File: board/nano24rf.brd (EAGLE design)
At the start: 17.8 x 40.3 mm, 18 parts

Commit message: ready for raw jumoper"
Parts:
- removed SJ4: JUMPER-PAD-3-2OF3_NC_BY_TRACE_LARGE, ATTAMI-V0.00:PAD-JUMPER-3-2OF3_NC_BY_TRACE_YES_SILK_LARGE
- added SJ2: (no value), microbuilder:SOLDERJUMPER_REFLOW
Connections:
- removed net N$6: D1.1, D2.1, FET1.1, FET2.1, SJ4.2
- net RAW: now also SJ2.1; no longer SJ4.3
- net VOUT: now also D1.1, D2.1, FET1.1, FET2.1, SJ2.2; no longer SJ4.1
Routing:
- net N$6: track 14.6 -> 0.00 mm
- net RAW: track 37.7 -> 32.9 mm
- net VOUT: track 22.8 -> 24.4 mm
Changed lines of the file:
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@@
 <wire x1="0" y1="40.31" x2="0" y2="0" width="0" layer="20"/>
 <text x="4.445" y="30.48" size="1.27" layer="21" font="vector">SEshenkar</text>
-<text x="5.715" y="37.973" size="1.27" layer="21" font="vector">nano24RF</text>
-<text x="10.795" y="36.703" size="0.8128" layer="21" font="vector">v1</text>
+<text x="4.445" y="37.973" size="1.27" layer="21" font="vector">nano24RF</text>
+<text x="10.16" y="36.703" size="0.8128" layer="21" font="vector">v1</text>
 <wire x1="6.477" y1="0.889" x2="6.985" y2="0.889" width="0.254" layer="21"/>
 <wire x1="7.493" y1="0.889" x2="6.985" y2="0.889" width="0.254" layer="21"/>
@@
 <attribute name="VALUE" x="13.335" y="39.37" size="0.4064" layer="27" ratio="10" rot="R270"/>
 </element>
-<element name="SJ4" library="ATTAMI-V0.00" package="PAD-JUMPER-3-2OF3_NC_BY_TRACE_YES_SILK_LARGE" value="JUMPER-PAD-3-2OF3_NC_BY_TRACE_LARGE" x="8.255" y="10.795" smashed="yes" rot="R180">
-<attribute name="NAME" x="10.922" y="12.065" size="1.016" layer="25" font="vector" ratio="10" rot="R270"/>
-<attribute name="VALUE" x="8.3551" y="10.795" size="0.02" layer="27" rot="R180"/>
-</element>
+<element name="SJ2" library="microbuilder" package="SOLDERJUMPER_REFLOW" value="" x="5.08" y="-1.905"/>
 </elements>
 <signals>
@@
 <contactref element="JP1" pad="15"/>
 <contactref element="SJ1" pad="1"/>
-<contactref element="SJ4" pad="3"/>
 <wire x1="8.255" y1="28.702" x2="8.255" y2="28.31" width="0.4064" layer="1"/>
 <wire x1="8.255" y1="28.31" x2="9.895" y2="26.67" width="0.4064" layer="1"/>
@@
 <wire x1="1.27" y1="2.54" x2="5.715" y2="8.89" width="1.016" layer="16"/>
 <via x="5.715" y="8.89" extent="1-16" drill="0.6" shape="square"/>
-<wire x1="5.715" y1="8.89" x2="6.731" y2="10.795" width="1.016" layer="1" curve="13.839067"/>
-<wire x1="6.731" y1="10.795" x2="8.001" y2="13.081" width="0.6096" layer="1" curve="-15.803299"/>
 <via x="8.001" y="13.081" extent="1-16" drill="0.6" shape="square"/>
 <wire x1="8.001" y1="13.081" x2="8.001" y2="15.113" width="0.6096" layer="16" curve="73.912494"/>
@@
 <wire x1="11.049" y1="28.956" x2="11.049" y2="27.824" width="0.6096" layer="1"/>
 <wire x1="11.049" y1="27.824" x2="9.895" y2="26.67" width="0.6096" layer="1"/>
+<contactref element="SJ2" pad="1"/>
+<wire x1="5.715" y1="8.89" x2="8.001" y2="13.081" width="0" layer="19" extent="1-1"/>
+<wire x1="4.318" y1="-1.905" x2="1.27" y2="2.54" width="0" layer="19" extent="1-1"/>
 </signal>
 <signal name="N$2">
@@
 <contactref element="C2" pad="1"/>
 <contactref element="R4" pad="1"/>
-<contactref element="SJ4" pad="1"/>
 <wire x1="5.3" y1="24.765" x2="8.1" y2="24.765" width="0.4064" layer="1"/>
 <wire x1="8.1" y1="24.765" x2="10.16" y2="25.03" width="0.4064" layer="1"/>
@@
 <wire x1="13.208" y1="22.479" x2="13.208" y2="21.336" width="0.6096" layer="1" curve="13.746918"/>
 <wire x1="8.89" y1="17.78" x2="9.525" y2="13.081" width="0.6096" layer="1"/>
-<wire x1="9.525" y1="13.081" x2="9.779" y2="10.795" width="0.6096" layer="1" curve="-2.71172"/>
+<contactref element="D2" pad="1"/>
+<contactref element="FET2" pad="1"/>
+<wire x1="10.085" y1="6.35" x2="10.795" y2="2.54" width="1.016" layer="1"/>
+<contactref element="FET1" pad="1"/>
+<contactref element="D1" pad="1"/>
+<contactref element="SJ2" pad="2"/>
+<wire x1="10.085" y1="6.35" x2="9.525" y2="13.081" width="0" layer="19" extent="1-1"/>
+<wire x1="7.695" y1="6.35" x2="10.085" y2="6.35" width="0" layer="19" extent="1-1"/>
+<wire x1="6.985" y1="2.54" x2="10.795" y2="2.54" width="0" layer="19" extent="1-1"/>
+<wire x1="5.842" y1="-1.905" x2="6.985" y2="2.54" width="0" layer="19" extent="1-1"/>
 </signal>
 <signal name="N$7">
@@
 <wire x1="15.24" y1="8.509" x2="16.51" y2="7.62" width="0.4064" layer="16" curve="82.225714"/>
 </signal>
-<signal name="N$6">
-<contactref element="FET1" pad="1"/>
-<contactref element="D1" pad="1"/>
-<contactref element="SJ4" pad="2"/>
-<contactref element="D2" pad="1"/>
-<contactref element="FET2" pad="1"/>
-<wire x1="8.255" y1="10.795" x2="7.695" y2="6.35" width="1.016" layer="1"/>
-<wire x1="7.695" y1="6.35" x2="10.085" y2="6.35" width="1.016" layer="1"/>
-<wire x1="10.085" y1="6.35" x2="10.795" y2="2.54" width="1.016" layer="1"/>
-<wire x1="10.795" y1="2.54" x2="6.985" y2="2.54" width="1.016" layer="1"/>
-</signal>
 </signals>

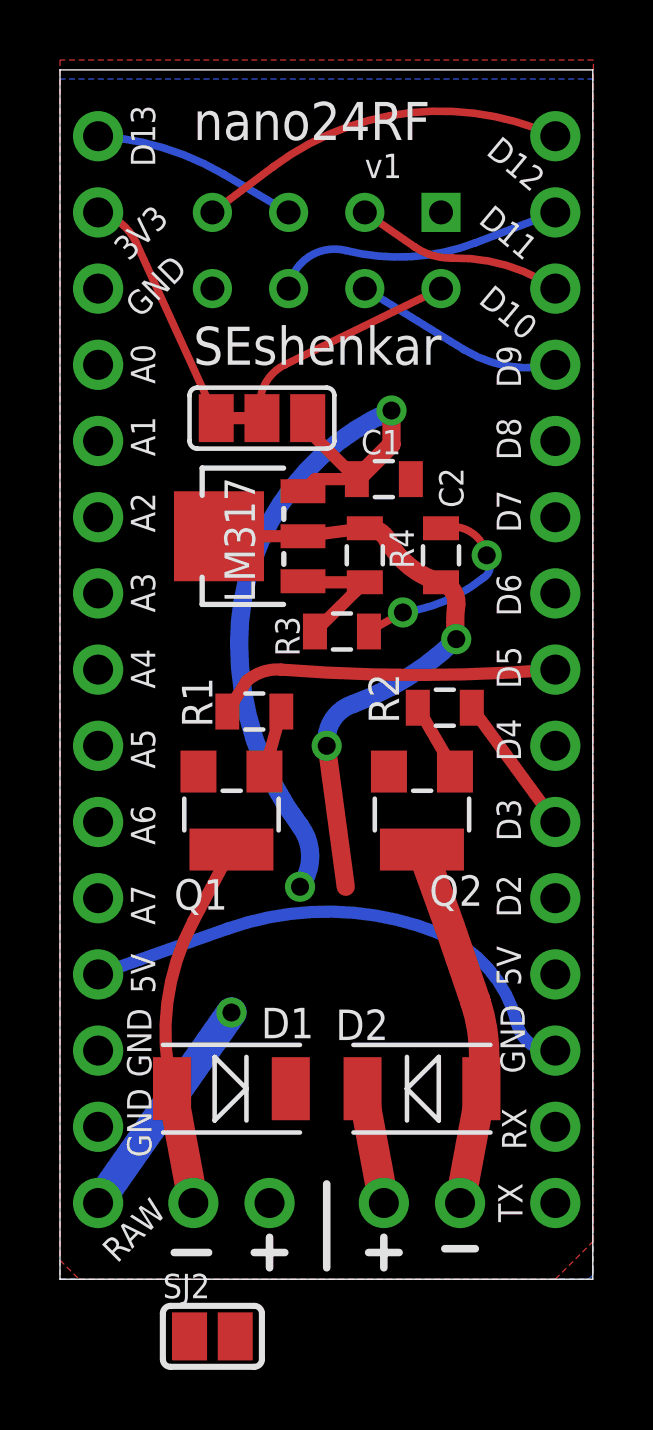
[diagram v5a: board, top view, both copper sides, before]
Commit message: removed lm317 and placed msfets on bottom
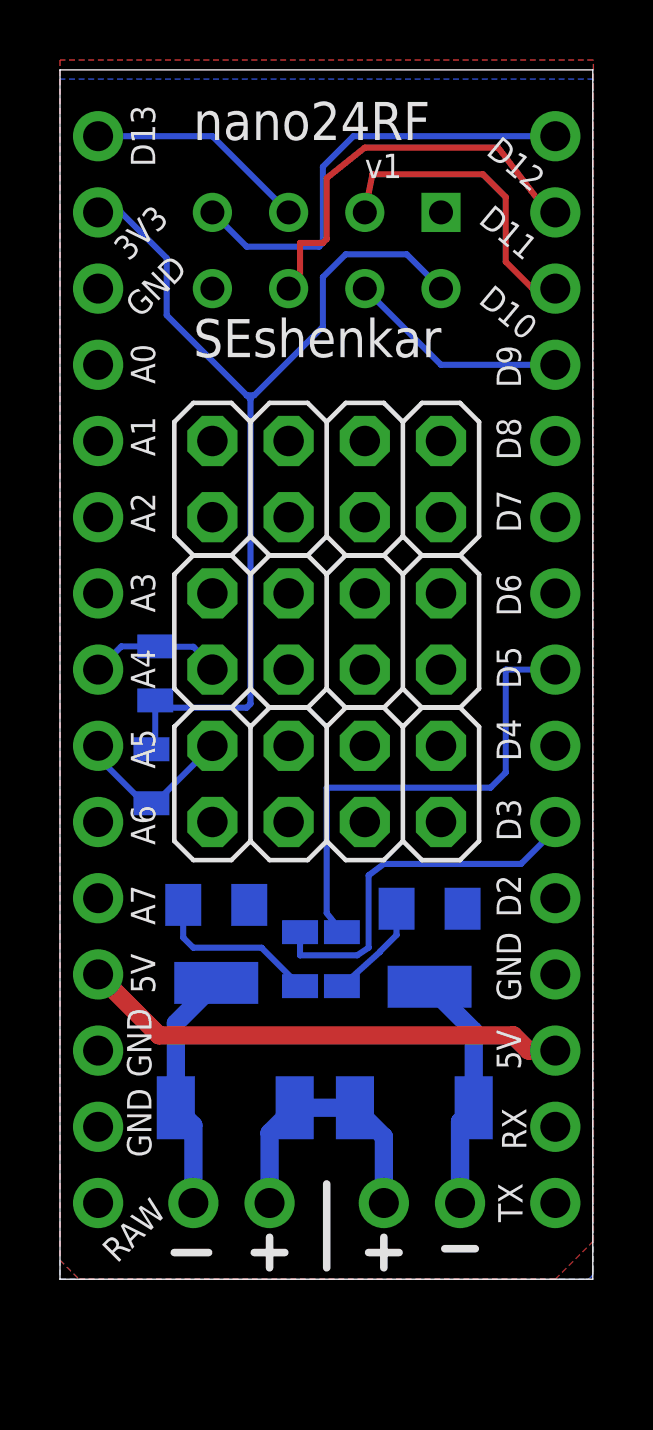
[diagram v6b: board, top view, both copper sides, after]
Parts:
- removed C1: 0.1uF, ATTAMI-V0.00:0805
- removed C2: 1uF, ATTAMI-V0.00:0805
- removed LM317: (no value), ATTAMI-V0.00:SOT89
- removed SJ1: JUMPER-PAD-3-2OF3_NC_BY_TRACE_LARGE, ATTAMI-V0.00:PAD-JUMPER-3-2OF3_NC_BY_TRACE_YES_SILK_LARGE
- removed SJ2: (no value), microbuilder:SOLDERJUMPER_REFLOW
- added JP3, JP4, JP5: (no value), adafruit:2X04
- moved R4 10.2 mm to (3.05, 16.8), flipped to the bottom, turned to 90 degrees
- moved R2 9.67 mm to (8.00, 10.7), flipped to the bottom, turned to 270 degrees
- moved R1 8.76 mm to (9.40, 10.7), flipped to the bottom, turned to 270 degrees
- moved Q2 8.17 mm to (5.21, 11.2), flipped to the bottom
- moved Q1 8.03 mm to (12.3, 11.0), flipped to the bottom
- moved R3 6.38 mm to (3.17, 20.2), flipped to the bottom, turned to 270 degrees
- moved FET1 6.35 mm to (12.1, 2.54), turned to 0 degrees
- moved FET2 6.35 mm to (5.71, 2.54), turned to 180 degrees
- moved D2 6.26 mm to (5.84, 5.71), flipped to the bottom
- moved D1 6.13 mm to (11.8, 5.71), flipped to the bottom
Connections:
- removed net N$7: LM317.GND, R3.2, R4.2
- new net SCL: JP1.9, JP4.2, R4.1
- new net SDA: JP1.8, JP3.1, R3.1
- net 3V3: now also R3.2, R4.2; no longer SJ1.2, SJ1.3
- net GND: no longer C1.2, C2.2, R3.1
- net RAW: no longer C1.1, LM317.VIN, SJ1.1, SJ2.1
- net VOUT: no longer C2.1, LM317.VOUT@1, LM317.VOUT@2, R4.1, SJ2.2
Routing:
- net RAW: track 32.9 -> 0.00 mm, vias 3 -> 0
- net 3V3: track 15.8 -> 33.8 mm
- net VOUT: track 24.4 -> 9.10 mm, vias 2 -> 0
- net D3: track 4.72 -> 12.6 mm
- net GND: track 6.74 -> 0.00 mm, vias 2 -> 0
- net SCL: track 0.00 -> 5.62 mm
- net D5: track 11.6 -> 16.3 mm
- net SDA: track 0.00 -> 4.52 mm
- net N$7: track 4.41 -> 0.00 mm
- net MOSI: track 9.47 -> 13.7 mm
- net N$1: track 12.2 -> 8.01 mm
- net N$4: track 12.2 -> 8.13 mm
- net CE: track 6.91 -> 10.2 mm
- net N$5: track 2.46 -> 5.65 mm
- net MISO: track 12.0 -> 14.9 mm
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
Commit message: wsitch!
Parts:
- added JP6: (no value), ATTAMI-V0.00:1X02_ROUND
- added SW1: (no value), microbuilder:SPST_SMT_19192
- moved FET1 7.77 mm to (10.5, -5.08)
- moved FET2 7.77 mm to (4.19, -5.08)
- moved D1 4.83 mm to (11.7, 0.89)
- moved D2 4.83 mm to (5.84, 0.89)
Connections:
- removed net VOUT: D1.1, D2.1, FET1.1, FET2.1
- new net VIN: D1.1, D2.1, FET1.1, FET2.1, JP1.15, SW1.C
- net GND: now also JP6.2; no longer JP1.13
- net RAW: now also JP6.1, SW1.B; no longer JP1.15
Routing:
- net VIN: track 0.00 -> 32.6 mm, vias 0 -> 1
- net RAW: track 0.00 -> 13.0 mm
- net VOUT: track 9.10 -> 0.00 mm
- net N$1: track 8.01 -> 16.4 mm
- net N$4: track 8.13 -> 15.7 mm
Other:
- board size 17.8 x 40.3 mm -> 17.8 x 47.8 mm
- board text added: "OFF|ON"
- board text added: "RST"
- board text added: "VIN"

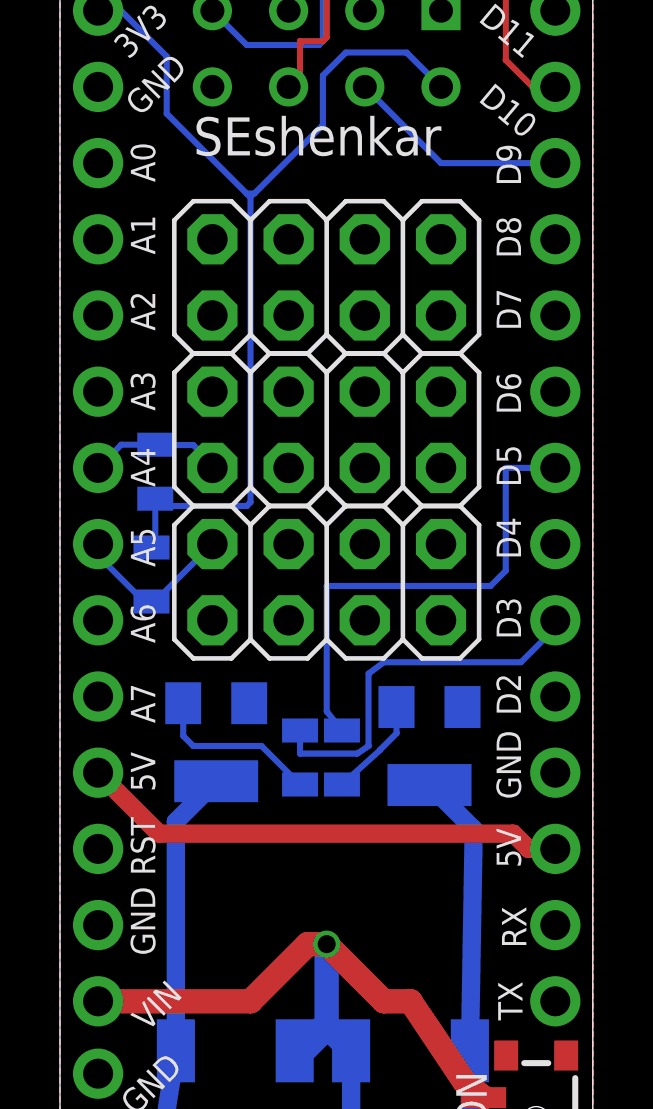
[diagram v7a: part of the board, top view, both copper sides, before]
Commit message: slikscreens
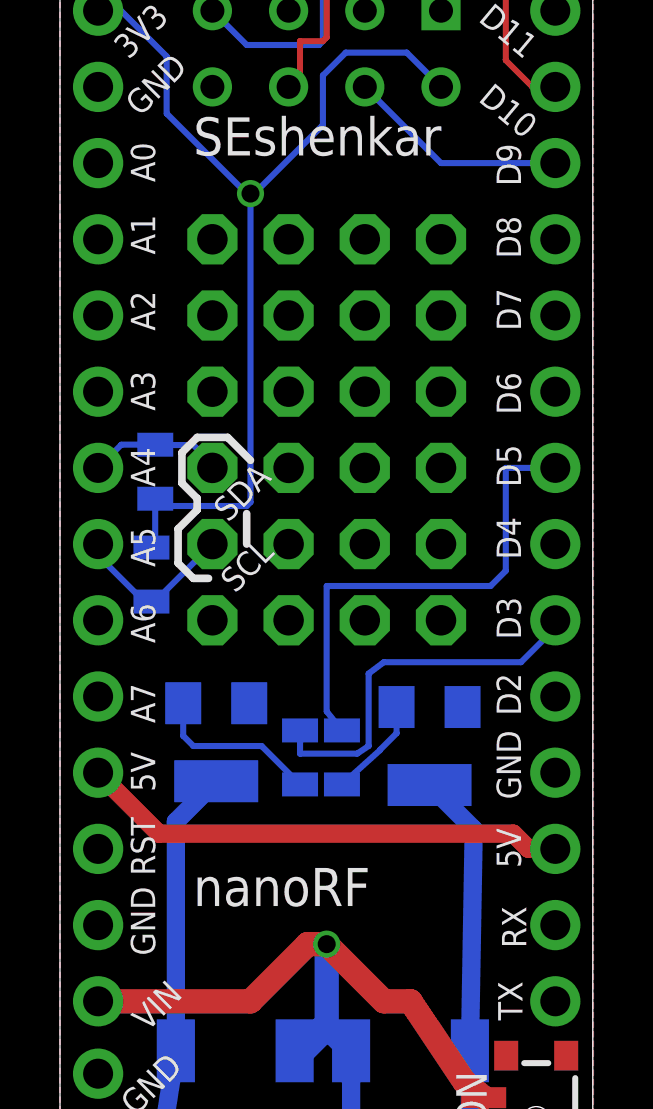
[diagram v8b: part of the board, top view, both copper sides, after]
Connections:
- net 3V3 renamed SHIOW
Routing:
- net SHIOW: vias 0 -> 1
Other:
- board text added: "SCL"
- board text added: "SDA"
- board text added: "nanoRF"
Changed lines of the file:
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@@
 <text x="3.81" y="-1.397" size="0.8128" layer="21" font="vector" rot="R225">RAW</text>
 <text x="13.208" y="-4.572" size="1.016" layer="21" font="vector" distance="212" rot="R270" align="bottom-right">OFF|ON</text>
+<text x="6.604" y="18.034" size="0.8128" layer="21" font="vector" rot="R225">SCL</text>
+<text x="6.514196875" y="20.5368" size="0.8128" layer="21" font="vector" rot="R225">SDA</text>
+<wire x1="4.953" y1="16.637" x2="4.445" y2="16.637" width="0.254" layer="21"/>
+<wire x1="4.445" y1="16.637" x2="3.937" y2="17.145" width="0.254" layer="21"/>
+<wire x1="3.937" y1="17.145" x2="3.937" y2="18.288" width="0.254" layer="21"/>
+<wire x1="3.937" y1="18.288" x2="4.572" y2="18.923" width="0.254" layer="21"/>
+<wire x1="4.572" y1="18.923" x2="4.572" y2="19.304" width="0.254" layer="21"/>
+<wire x1="4.572" y1="19.304" x2="4.064" y2="19.812" width="0.254" layer="21"/>
+<wire x1="4.064" y1="19.812" x2="4.064" y2="20.828" width="0.254" layer="21"/>
+<wire x1="4.064" y1="20.828" x2="4.572" y2="21.336" width="0.254" layer="21"/>
+<wire x1="4.572" y1="21.336" x2="5.588" y2="21.336" width="0.254" layer="21"/>
+<wire x1="5.588" y1="21.336" x2="6.35" y2="20.574" width="0.254" layer="21"/>
+<wire x1="6.223" y1="18.796" x2="6.223" y2="17.78" width="0.254" layer="21"/>
+<text x="4.445" y="5.715" size="1.27" layer="21" font="vector">nanoRF</text>
 </plain>
 <attributes>
@@
 <contactref element="JP2" pad="7"/>
 </signal>
-<signal name="3V3">
+<signal name="SHIOW">
 <contactref element="JP1" pad="2"/>
 <contactref element="U$2" pad="VCC"/>
@@
 <wire x1="8.763" y1="33.401" x2="8.763" y2="31.75" width="0.2032" layer="16"/>
 <wire x1="8.763" y1="31.75" x2="6.477" y2="29.464" width="0.2032" layer="16"/>
-<wire x1="6.477" y1="29.464" x2="6.223" y2="29.464" width="0.2032" layer="16"/>
+<wire x1="6.477" y1="29.464" x2="6.35" y2="29.464" width="0.2032" layer="16"/>
+<wire x1="6.35" y1="29.464" x2="6.223" y2="29.464" width="0.2032" layer="16"/>
+<via x="6.35" y="29.464" extent="1-16" drill="0.6" shape="square"/>
 </signal>
 <signal name="MISO">
